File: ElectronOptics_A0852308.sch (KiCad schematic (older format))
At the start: 0 parts

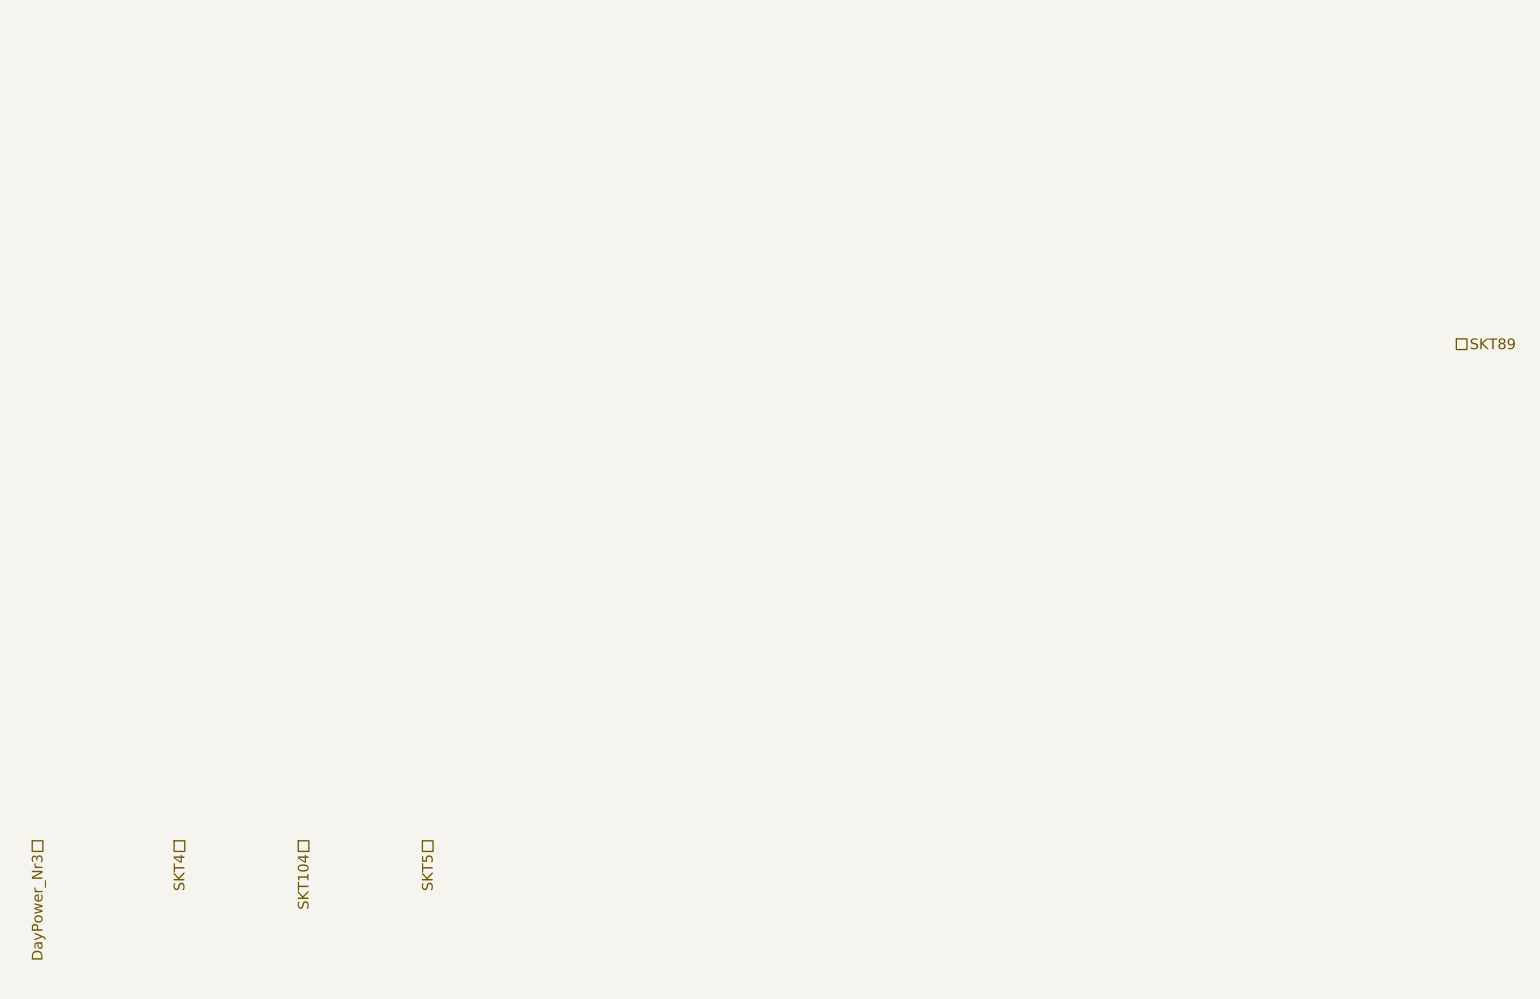
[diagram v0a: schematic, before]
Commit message: Adds Electron Optics PCB
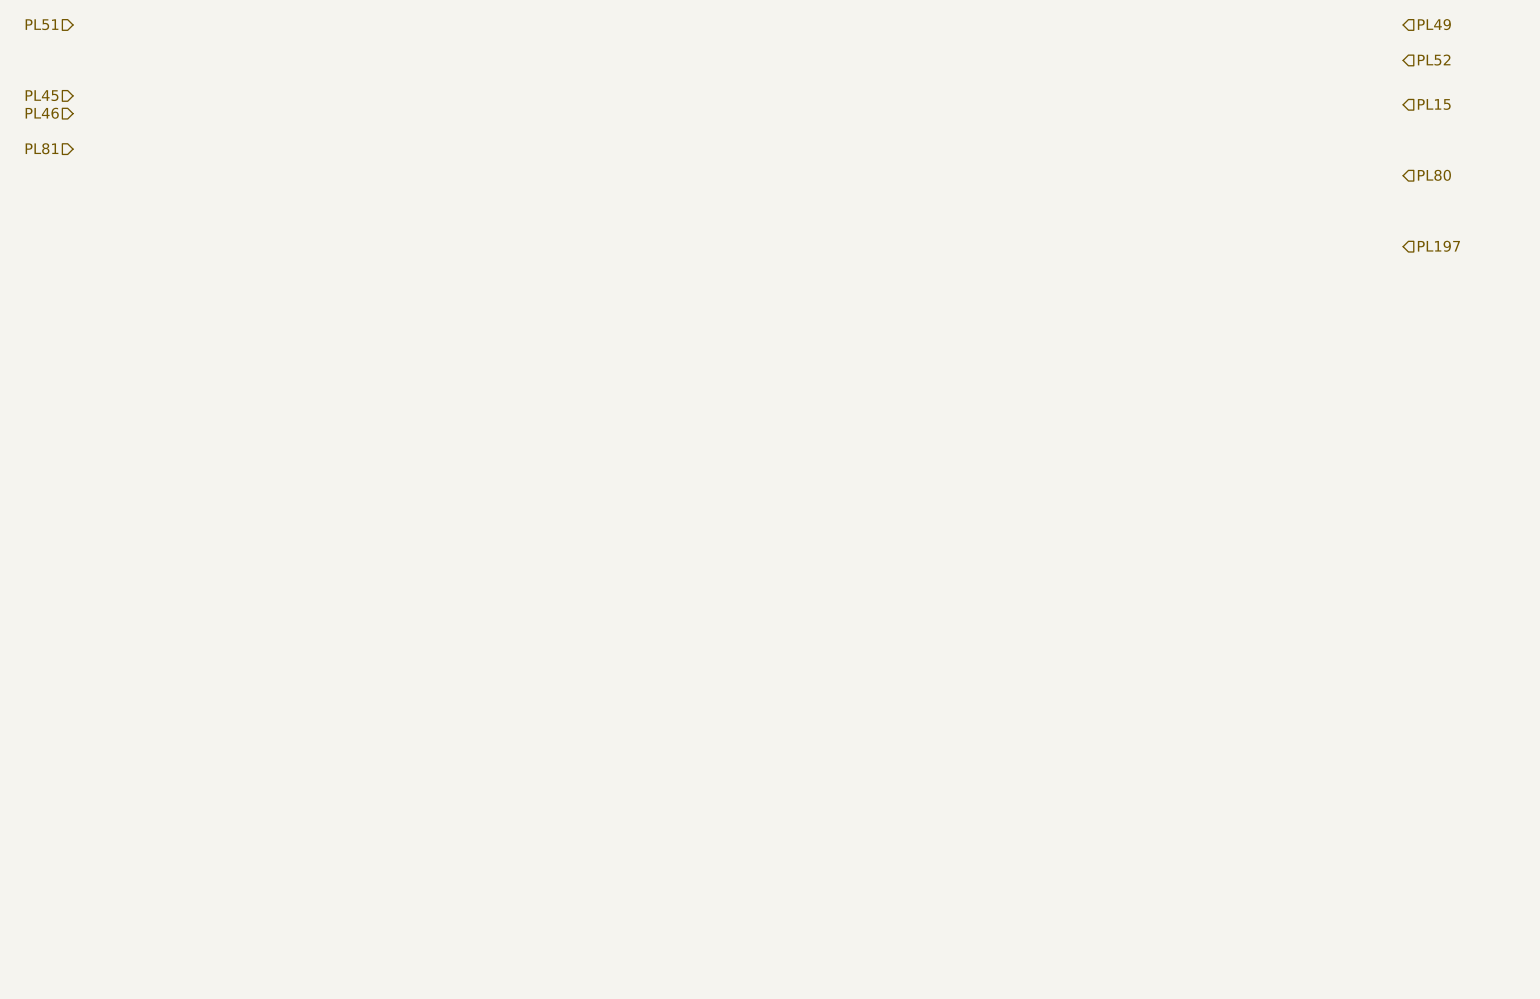
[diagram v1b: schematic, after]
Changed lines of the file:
@@
 $Descr A4 11693 8268
 encoding utf-8
-Sheet 5 17
+Sheet 17 17
 Title ""
 Date ""
@@
 Comment4 ""
 $EndDescr
-Text HLabel 1500 6100 3    60   UnSpc ~ 0
-DayPower_Nr3
-Text HLabel 2300 6100 3    60   UnSpc ~ 0
-SKT4
-Text HLabel 3000 6100 3    60   UnSpc ~ 0
-SKT104
-Text HLabel 3700 6100 3    60   UnSpc ~ 0
-SKT5
-Text HLabel 9500 3300 2    60   UnSpc ~ 0
-SKT89
+Text HLabel 1700 1500 0    60   Input ~ 0
+PL51
+Text HLabel 1700 1900 0    60   Input ~ 0
+PL45
+Text HLabel 9200 1500 2    60   Input ~ 0
+PL49
+Text HLabel 9200 1950 2    60   Input ~ 0
+PL15
+Text HLabel 9200 2350 2    60   Input ~ 0
+PL80
+Text HLabel 1700 2200 0    60   Input ~ 0
+PL81
+Text HLabel 9200 2750 2    60   Input ~ 0
+PL197
+Text HLabel 1700 2000 0    60   Input ~ 0
+PL46
+Text HLabel 9200 1700 2    60   Input ~ 0
+PL52
 $EndSCHEMATC

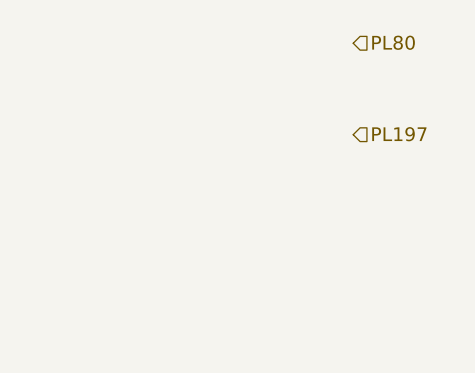
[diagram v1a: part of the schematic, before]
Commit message: Wired up Electron Optics
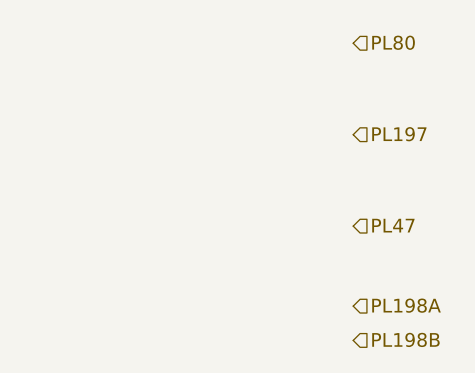
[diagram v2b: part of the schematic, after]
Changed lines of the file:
@@
 Text HLabel 9200 1700 2    60   Input ~ 0
 PL52
+Text HLabel 9200 3150 2    60   Input ~ 0
+PL47
+Text HLabel 9200 3500 2    60   Input ~ 0
+PL198A
+Text HLabel 9200 3650 2    60   Input ~ 0
+PL198B
 $EndSCHEMATC
